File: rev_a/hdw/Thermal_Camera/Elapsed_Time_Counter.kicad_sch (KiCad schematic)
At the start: 14 parts, among them J2301 I2C, J2302 UART, J2303 VOSPI, J2304 FLASH SPI

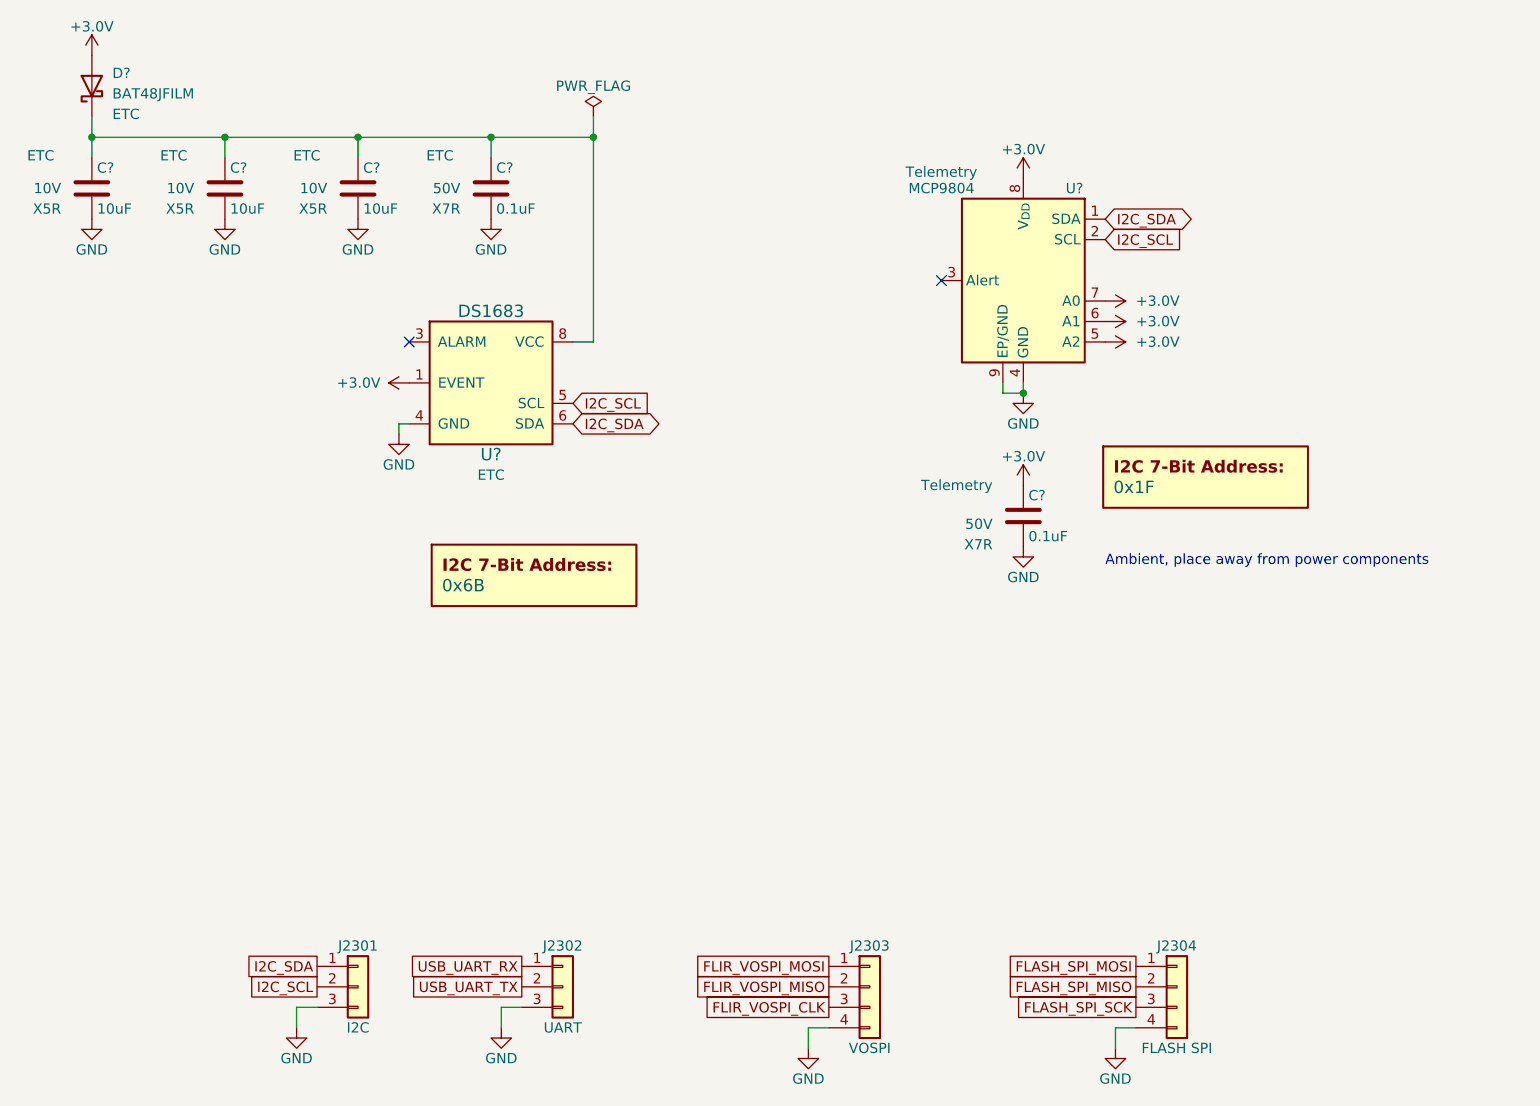
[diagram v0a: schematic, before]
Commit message: assigned a ton of footprints
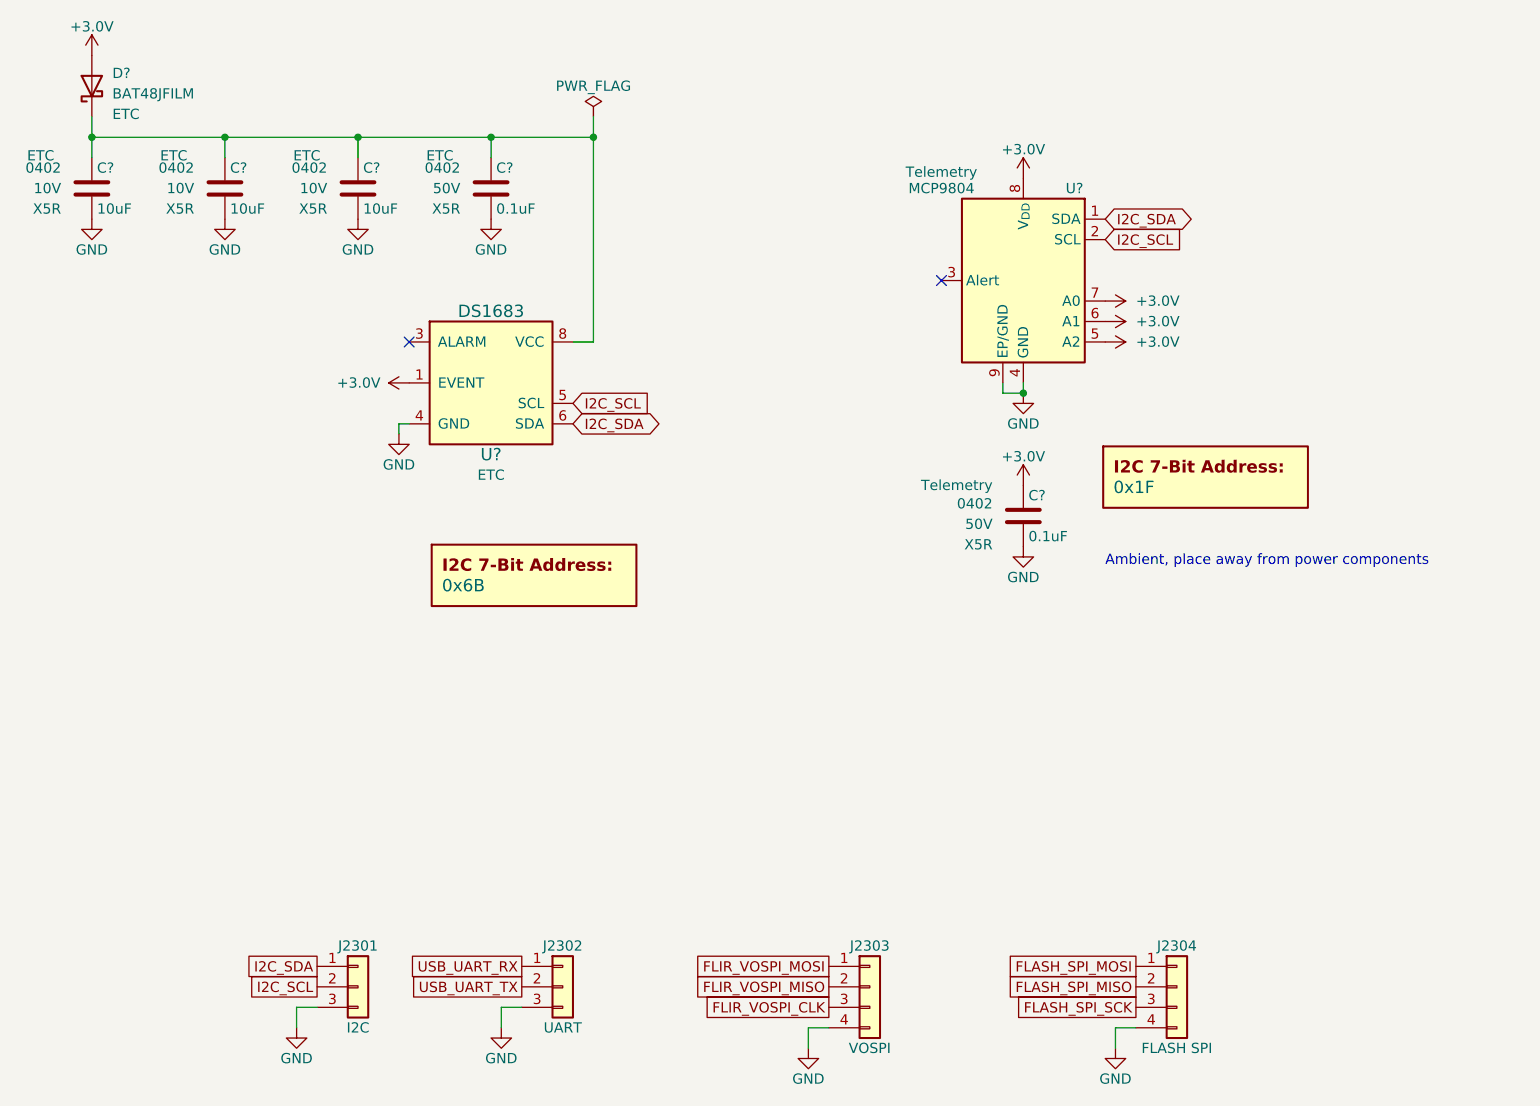
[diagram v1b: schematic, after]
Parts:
- C? (x3): footprint (none) -> Capacitors_SMD:C_0402; display_footprint (none) -> 0402
- C? (x2): footprint (none) -> Capacitors_SMD:C_0402; Dielectric X7R -> X5R; display_footprint (none) -> 0402
- J2301, J2302: footprint (none) -> Connector_PinHeader_2.54mm:PinHeader_1x03_P2.54mm_Vertical
- J2303, J2304: footprint (none) -> Connector_PinHeader_2.54mm:PinHeader_1x04_P2.54mm_Vertical
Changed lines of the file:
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@@
 			)
 		)
-		(property "Footprint" ""
+		(property "Footprint" "Capacitors_SMD:C_0402"
 			(at 87.3252 49.53 0)
 			(effects
@@
 			)
 		)
-		(property "display_footprint" ""
+		(property "display_footprint" "0402"
 			(at 82.55 43.18 0)
 			(effects
@@
 			)
 		)
-		(property "Footprint" ""
+		(property "Footprint" "Connector_PinHeader_2.54mm:PinHeader_1x04_P2.54mm_Vertical"
 			(at 149.86 144.78 0)
 			(effects
@@
 			)
 		)
-		(property "Footprint" ""
+		(property "Footprint" "Connector_PinHeader_2.54mm:PinHeader_1x04_P2.54mm_Vertical"
 			(at 187.96 144.78 0)
 			(effects
@@
 			)
 		)
-		(property "Footprint" ""
+		(property "Footprint" "Capacitors_SMD:C_0402"
 			(at 54.3052 49.53 0)
 			(effects
@@
 			)
 		)
-		(property "display_footprint" ""
+		(property "display_footprint" "0402"
 			(at 49.53 43.18 0)
 			(effects
@@
 			)
 		)
-		(property "Footprint" ""
+		(property "Footprint" "Connector_PinHeader_2.54mm:PinHeader_1x03_P2.54mm_Vertical"
 			(at 86.36 144.78 0)
 			(effects
@@
 			)
 		)
-		(property "Footprint" ""
+		(property "Footprint" "Capacitors_SMD:C_0402"
 			(at 103.8352 49.53 0)
 			(effects
@@
 			)
 		)
-		(property "display_footprint" ""
+		(property "display_footprint" "0402"
 			(at 99.06 43.18 0)
 			(effects
@@
 			)
 		)
-		(property "Dielectric" "X7R"
+		(property "Dielectric" "X5R"
 			(at 99.06 48.26 0)
 			(effects
@@
 			)
 		)
-		(property "Footprint" ""
+		(property "Footprint" "Capacitors_SMD:C_0402"
 			(at 70.8152 49.53 0)
 			(effects
@@
 			)
 		)
-		(property "display_footprint" ""
+		(property "display_footprint" "0402"
 			(at 66.04 43.18 0)
 			(effects
@@
 			)
 		)
-		(property "Footprint" ""
+		(property "Footprint" "Connector_PinHeader_2.54mm:PinHeader_1x03_P2.54mm_Vertical"
 			(at 111.76 144.78 0)
 			(effects
@@
 			)
 		)
-		(property "Footprint" ""
+		(property "Footprint" "Capacitors_SMD:C_0402"
 			(at 169.8752 90.17 0)
 			(effects
@@
 			)
 		)
-		(property "display_footprint" ""
+		(property "display_footprint" "0402"
 			(at 165.1 84.836 0)
 			(effects
@@
 			)
 		)
-		(property "Dielectric" "X7R"
+		(property "Dielectric" "X5R"
 			(at 165.1 89.916 0)
 			(effects

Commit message: assigned some part numbers
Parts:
- C? (x3): Digi-Key PN (none) -> 490-GRM155R61A106ME11DCT-ND
- C? (x2): Digi-Key PN (none) -> 490-10697-1-ND
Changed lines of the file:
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@@
 			)
 		)
-		(property "Digi-Key PN" ""
+		(property "Digi-Key PN" "490-GRM155R61A106ME11DCT-ND"
 			(at 97.155 33.02 0)
 			(effects
@@
 			)
 		)
-		(property "Digi-Key PN" ""
+		(property "Digi-Key PN" "490-GRM155R61A106ME11DCT-ND"
 			(at 64.135 33.02 0)
 			(effects
@@
 			)
 		)
-		(property "Digi-Key PN" ""
+		(property "Digi-Key PN" "490-10697-1-ND"
 			(at 102.87 45.72 0)
 			(effects
@@
 			)
 		)
-		(property "Digi-Key PN" ""
+		(property "Digi-Key PN" "490-GRM155R61A106ME11DCT-ND"
 			(at 80.645 33.02 0)
 			(effects
@@
 			)
 		)
-		(property "Digi-Key PN" ""
+		(property "Digi-Key PN" "490-10697-1-ND"
 			(at 168.91 86.36 0)
 			(effects

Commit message: finished placing components
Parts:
- removed J2301: I2C, Connector_PinHeader_2.54mm:PinHeader_1x03_P2.54mm_Vertical, symbol Connector_Generic:Conn_01x03
- removed J2302: UART, Connector_PinHeader_2.54mm:PinHeader_1x03_P2.54mm_Vertical, symbol Connector_Generic:Conn_01x03
- removed J2303: VOSPI, Connector_PinHeader_2.54mm:PinHeader_1x04_P2.54mm_Vertical, symbol Connector_Generic:Conn_01x04
- removed J2304: FLASH SPI, Connector_PinHeader_2.54mm:PinHeader_1x04_P2.54mm_Vertical, symbol Connector_Generic:Conn_01x04
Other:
- moved on the sheet: C?, D?, U?
